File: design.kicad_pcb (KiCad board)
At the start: 2 copper layers, 25 x 18 mm, 0 parts

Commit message: first layouts
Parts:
- added D1: SK6805_1515, LED_SMD:LED_SK6812_EC15_1.5x1.5mm, F.Cu at (154.8, 94.8)
- added D2: SK6805_1515, LED_SMD:LED_SK6812_EC15_1.5x1.5mm, F.Cu at (156.8, 94.8)
- added D3: SK6805_1515, LED_SMD:LED_SK6812_EC15_1.5x1.5mm, F.Cu at (158.8, 94.8)
- added D4: SK6805_1515, LED_SMD:LED_SK6812_EC15_1.5x1.5mm, F.Cu at (154.8, 96.8)
- added D5: SK6805_1515, LED_SMD:LED_SK6812_EC15_1.5x1.5mm, F.Cu at (156.8, 96.8)
- added D6: SK6805_1515, LED_SMD:LED_SK6812_EC15_1.5x1.5mm, F.Cu at (158.8, 96.8)
- added D7: SK6805_1515, LED_SMD:LED_SK6812_EC15_1.5x1.5mm, F.Cu at (154.8, 98.8)
- added D8: SK6805_1515, LED_SMD:LED_SK6812_EC15_1.5x1.5mm, F.Cu at (156.8, 98.8)
- added D9: SK6805_1515, LED_SMD:LED_SK6812_EC15_1.5x1.5mm, F.Cu at (158.8, 98.8)
- added J1: Conn_01x03_Female, Connector_PinHeader_2.54mm:PinHeader_1x03_P2.54mm_Horizontal, F.Cu at (147.4, 98.5)
- added R1: 500, Resistor_SMD:R_0805_2012Metric, F.Cu at (150.0, 91.0)
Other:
- board size 25 x 18 mm -> 20 x 10 mm

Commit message: scramble
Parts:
- J1: footprint Connector_PinHeader_2.54mm:PinHeader_1x03_P2.54mm_Horizontal -> Connector_PinHeader_2.54mm:PinHeader_1x03_P2.54mm_Vertical
- moved R1 4.47 mm to (152.0, 95.0), turned to 90 degrees
- moved D1 2.15 mm to (157.0, 94.8)
- moved D2 2.15 mm to (159.0, 94.8)
- moved D3 2.15 mm to (161.0, 94.8)
- moved D4 2.15 mm to (157.0, 96.8)
- moved D5 2.15 mm to (159.0, 96.8)
- moved D6 2.15 mm to (161.0, 96.8)
- moved D7 2.15 mm to (157.0, 98.8)
- moved D8 2.15 mm to (159.0, 98.8)
- moved D9 2.15 mm to (161.0, 98.8)
- moved J1 0.79 mm to (148.0, 99.0)

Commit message: more initial layout
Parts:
- moved R1 1.12 mm to (152.5, 94.0), turned to 0 degrees
- moved D7 0.86 mm to (156.5, 99.5)
- moved D9 0.86 mm to (161.5, 99.5)
- moved D8 0.70 mm to (159.0, 99.5)
- moved D1 0.58 mm to (156.5, 94.5)
- moved D3 0.58 mm to (161.5, 94.5)
- moved J1 0.54 mm to (148.0, 99.5)
- moved D4 0.54 mm to (156.5, 97.0)
- moved D6 0.54 mm to (161.5, 97.0)
- moved D2 0.30 mm to (159.0, 94.5)
- moved D5 0.20 mm to (159.0, 97.0)
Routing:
- net VCC: track 0.00 -> 36.4 mm
- net GND: track 0.00 -> 17.7 mm
- net Net-(D6-Pad3): track 0.00 -> 10.3 mm, vias 0 -> 2
- net Net-(D3-Pad3): track 0.00 -> 10.2 mm, vias 0 -> 2
- net Net-(R1-Pad1): track 0.00 -> 9.57 mm
- net Net-(D1-Pad1): track 0.00 -> 2.66 mm
- net Net-(D1-Pad3): track 0.00 -> 1.97 mm
- net Net-(D8-Pad3): track 0.00 -> 1.97 mm
- net Net-(D7-Pad3): track 0.00 -> 1.97 mm
- net Net-(D5-Pad3): track 0.00 -> 1.97 mm
- net Net-(D4-Pad3): track 0.00 -> 1.97 mm
- net Net-(D2-Pad3): track 0.00 -> 1.97 mm
- added copper zone on B.Cu, net GND
- added copper zone on F.Cu, net GND

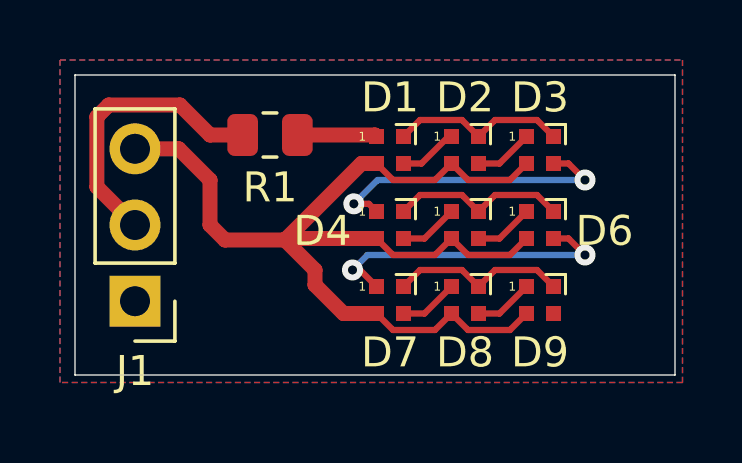
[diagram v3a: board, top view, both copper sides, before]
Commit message: changed to custom sk6805 footprint
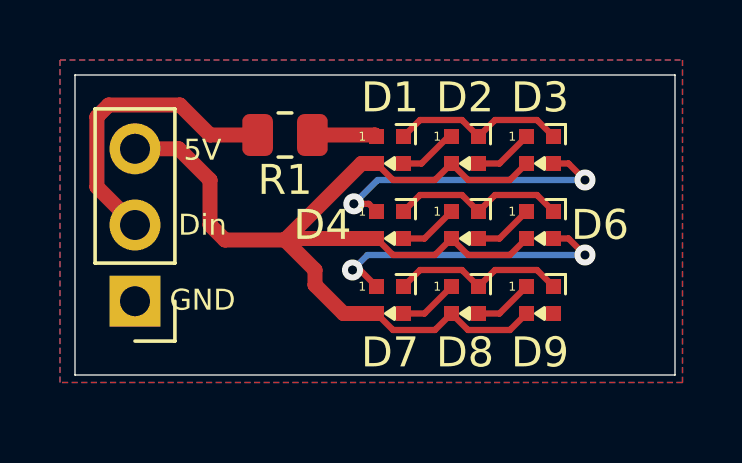
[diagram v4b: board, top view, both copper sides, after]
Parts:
- D1, D2, D3, D4, D5, D6, D7, D8, D9: footprint LED_SMD:LED_SK6812_EC15_1.5x1.5mm -> LED_custom:LED_SK6805_EC15_1.5x1.5mm
- moved R1 0.50 mm to (153.0, 94.0)
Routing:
- net Net-(R1-Pad1): track 9.57 -> 10.1 mm
- net Net-(D1-Pad1): track 2.66 -> 2.16 mm
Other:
- board text added: "5V"
- board text added: "Din"
- board text added: "GND"
